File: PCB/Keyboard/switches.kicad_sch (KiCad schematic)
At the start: 125 parts

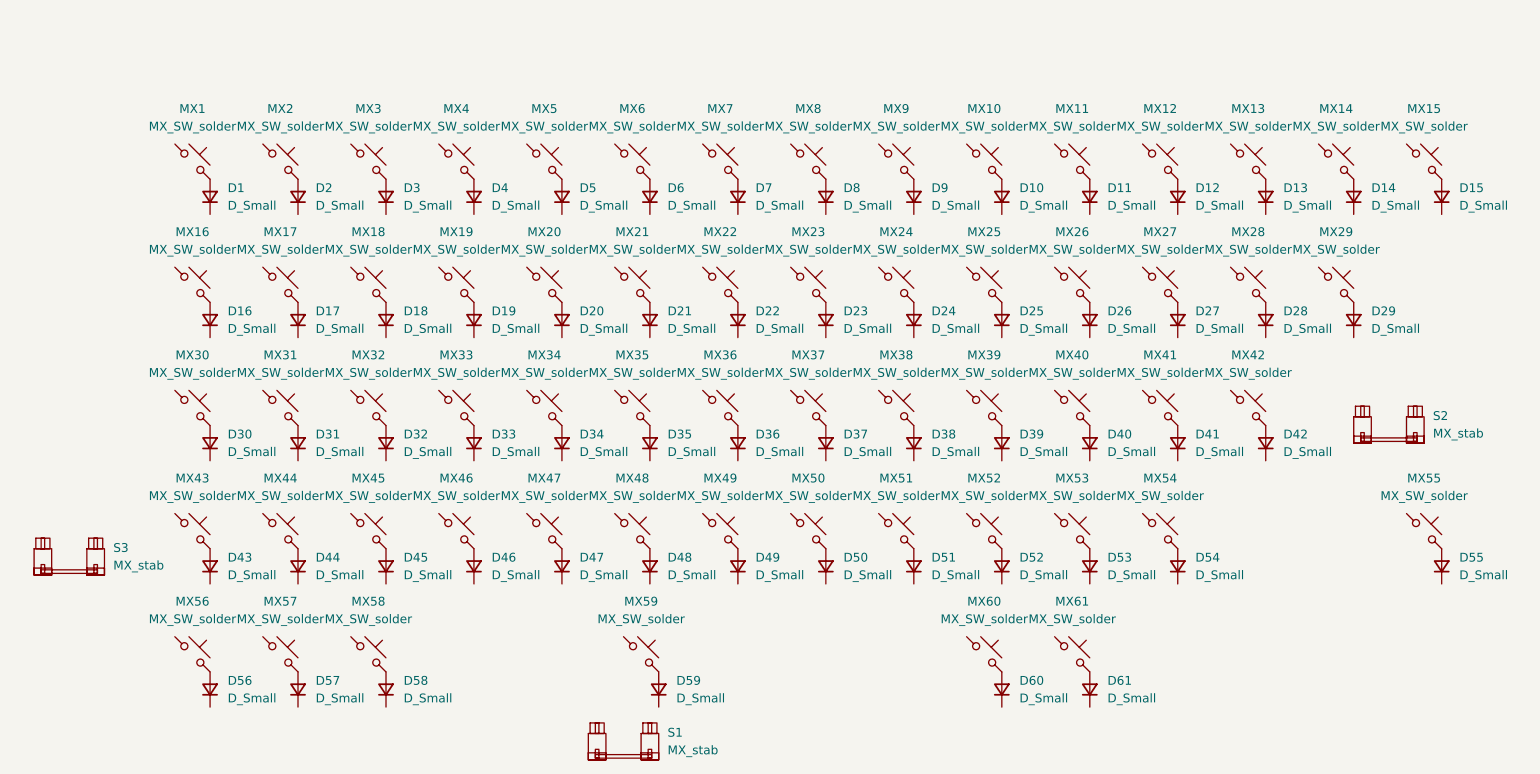
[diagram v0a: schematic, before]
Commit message: wire rows and cols
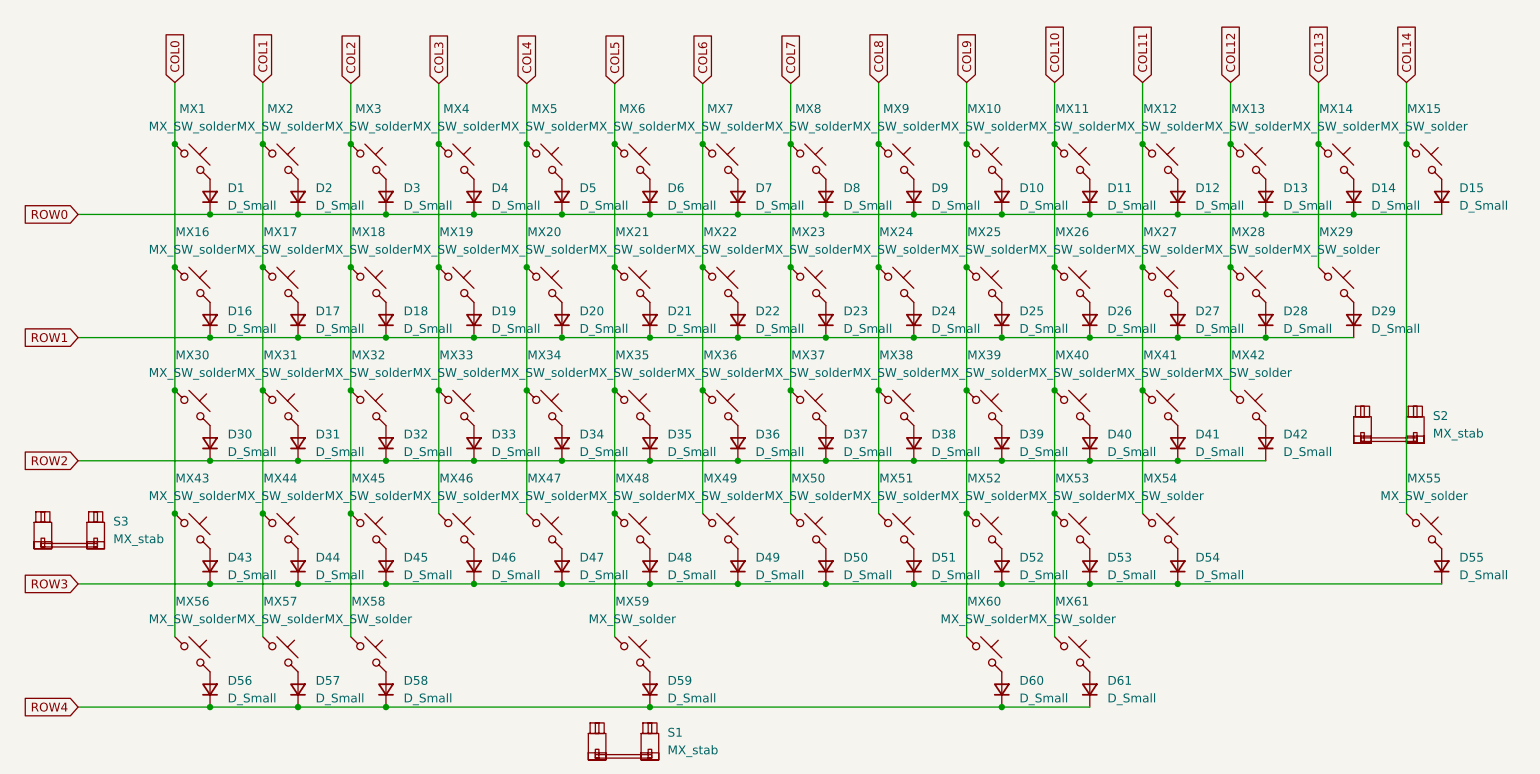
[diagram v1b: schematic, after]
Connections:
- net COL9: now reaches MX39.1
- net COL9: now also MX10.1, MX25.1, MX52.1, MX60.1
- net COL2: now reaches MX58.1
- net COL2: now also MX18.1, MX3.1, MX32.1, MX45.1
- net ROW3: now reaches D49.1 (K)
- net ROW3: now also D43.1 (K), D44.1 (K), D45.1 (K), D46.1 (K), D47.1 (K), D48.1 (K), D50.1 (K), D51.1 (K), D52.1 (K), D53.1 (K), D54.1 (K), D55.1 (K)
- net ROW1: now reaches D21.1 (K)
- net ROW1: now also D16.1 (K), D17.1 (K), D18.1 (K), D19.1 (K), D20.1 (K), D22.1 (K), D23.1 (K), D24.1 (K), D25.1 (K), D26.1 (K), D27.1 (K), D28.1 (K), D29.1 (K)
- net COL0: now reaches MX1.1
- net COL0: now also MX16.1, MX30.1, MX43.1, MX56.1
- net ROW0: now reaches D8.1 (K)
- net ROW0: now also D1.1 (K), D10.1 (K), D11.1 (K), D12.1 (K), D13.1 (K), D14.1 (K), D15.1 (K), D2.1 (K), D3.1 (K), D4.1 (K), D5.1 (K), D6.1 (K), D7.1 (K), D9.1 (K)
- net COL10: now reaches MX26.1
- net COL10: now also MX11.1, MX40.1, MX53.1, MX61.1
- net COL6: now reaches MX22.1
- net COL6: now also MX36.1, MX49.1, MX7.1
- net ROW2: now reaches D35.1 (K)
- net ROW2: now also D30.1 (K), D31.1 (K), D32.1 (K), D33.1 (K), D34.1 (K), D36.1 (K), D37.1 (K), D38.1 (K), D39.1 (K), D40.1 (K), D41.1 (K), D42.1 (K)
- net COL3: now reaches MX4.1
- net COL3: now also MX19.1, MX33.1, MX46.1
- net ROW4: now reaches D56.1 (K)
- net ROW4: now also D57.1 (K), D58.1 (K), D59.1 (K), D60.1 (K), D61.1 (K)
- net COL14: now reaches MX15.1
- net COL14: now also MX55.1
- net COL11: now reaches MX27.1
- net COL11: now also MX12.1, MX41.1, MX54.1
- net COL13: now reaches MX14.1
- net COL13: now also MX29.1
- net COL1: now reaches MX44.1
- net COL1: now also MX17.1, MX2.1, MX31.1, MX57.1
- net COL8: now reaches MX38.1
- net COL8: now also MX24.1, MX51.1, MX9.1
- net COL5: now reaches MX48.1
- net COL5: now also MX21.1, MX35.1, MX59.1, MX6.1
- net COL4: now reaches MX20.1
- net COL4: now also MX34.1, MX47.1, MX5.1
- net COL7: now reaches MX23.1
- net COL7: now also MX37.1, MX50.1, MX8.1
- net COL12: now reaches MX13.1
- net COL12: now also MX28.1, MX42.1
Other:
- moved on the sheet: D59, MX59, S3
